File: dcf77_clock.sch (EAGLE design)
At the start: 42 parts, among them IC1 7805DT, IC2 ATMEGA48/88/168-AU, J2 DCJ0202, Q1 32.768kHz, Q2 IRLML6244TRPBF, SW1 EC12E_SW, U1 LCD-16X2SILK, U2 DS1307SO8

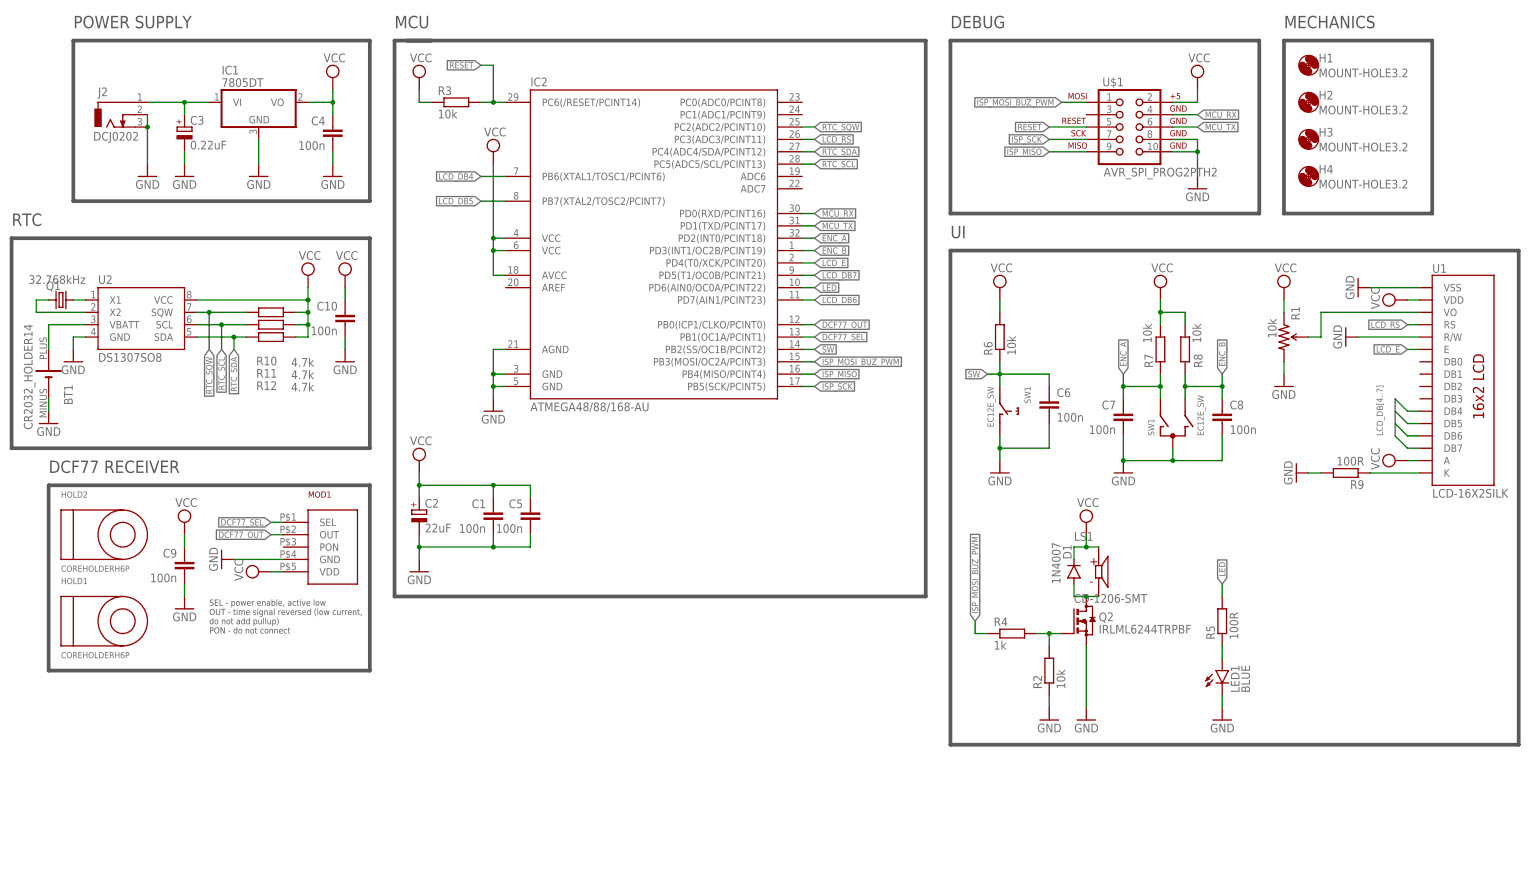
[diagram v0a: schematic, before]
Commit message: Finish signal and VCC routing
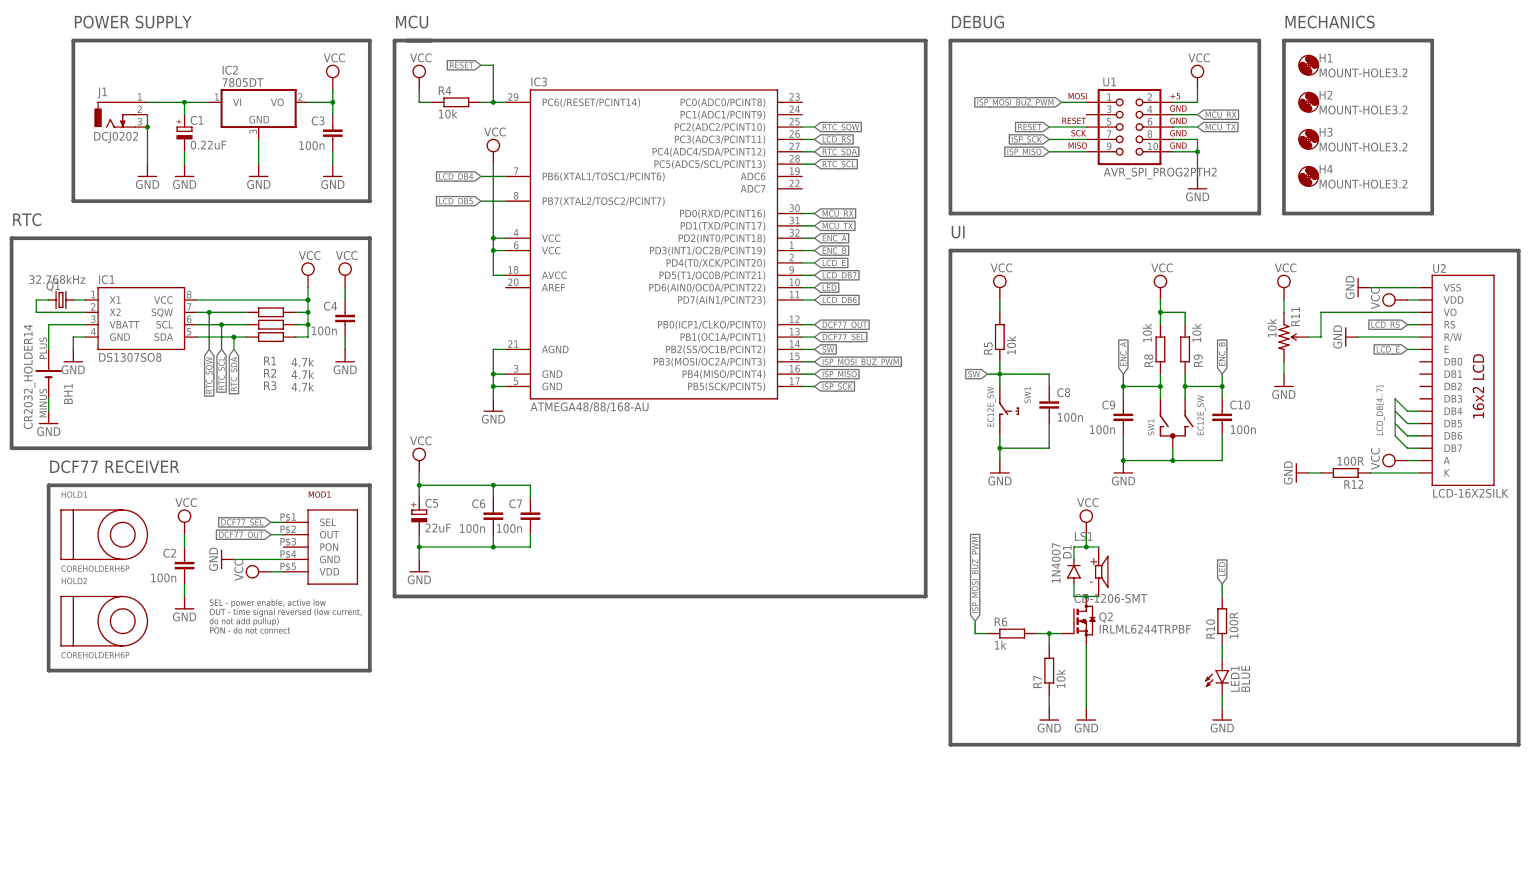
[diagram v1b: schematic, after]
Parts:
- removed U$1: AVR_SPI_PROG2PTH2, SparkFun:AVR_SPI_PROG2PTH2
- added IC3: ATMEGA48/88/168-AU, atmega8:ATMEGA48/88/168-AU
- C1: value 100n -> 0.22uF; device rcl:C-EUC0805K -> rcl:CPOL-EUSMCZ
- C2: value 22uF -> 100n; device rcl:CPOL-EUUD-4X5,8 -> rcl:C-EUC0805K
- C3: value 0.22uF -> 100n; device rcl:CPOL-EUSMCZ -> rcl:C-EUC0805K
- C5: value 100n -> 22uF; device rcl:C-EUC0805K -> rcl:CPOL-EUUD-4X5,8
- IC1: value 7805DT -> DS1307SO8; device linear:7805DT -> SparkFun:DS1307SO8
- IC2: value ATMEGA48/88/168-AU -> 7805DT; device atmega8:ATMEGA48/88/168-AU -> linear:7805DT
- R1: value 10k -> 4.7k; device SparkFun:TRIMPOTPTH -> rcl:R-EU_M0805
- R10, R12: value 4.7k -> 100R
- R11: value 4.7k -> 10k; device rcl:R-EU_M0805 -> SparkFun:TRIMPOTPTH
- R2, R3: value 10k -> 4.7k
- R4: value 1k -> 10k
- R5, R9: value 100R -> 10k
- R6: value 10k -> 1k
- U1: value LCD-16X2SILK -> AVR_SPI_PROG2PTH2; device SparkFun:LCD-16X2SILK -> SparkFun:AVR_SPI_PROG2PTH2
- U2: value DS1307SO8 -> LCD-16X2SILK; device SparkFun:DS1307SO8 -> SparkFun:LCD-16X2SILK
- renumbered BT1 to BH1, J2 to J1
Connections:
- net DCF77_OUT: now also IC3.PB0(ICP1/CLKO/PCINT0); no longer IC2.PB0(ICP1/CLKO/PCINT0)
- net DCF77_SEL: now also IC3.PB1(OC1A/PCINT1); no longer IC2.PB1(OC1A/PCINT1)
- net ENC_A: now also C9.1, IC3.PD2(INT0/PCINT18), R8.1; no longer C7.1, IC2.PD2(INT0/PCINT18), R7.1
- net ENC_B: now also C10.1, IC3.PD3(INT1/OC2B/PCINT19), R9.1; no longer C8.1, IC2.PD3(INT1/OC2B/PCINT19), R8.1
- net GND: now also C1.-, C2.2, C3.2, C5.-, IC2.GND, IC3.AGND, IC3.GND@1, IC3.GND@2, R11.CW, R12.2, R7.1, U1.10, U1.8, U2.R/W, U2.VSS; no longer C1.2, C2.-, C3.-, C5.2, IC2.AGND, IC2.GND@1, IC2.GND@2, R1.CW, R2.1, R9.2, U$1.10, U$1.8, U1.R/W, U1.VSS, U2.GND
- net ISP_MISO: now also IC3.PB4(MISO/PCINT4), U1.9; no longer IC2.PB4(MISO/PCINT4), U$1.9
- net ISP_MOSI_BUZ_PWM: now also IC3.PB3(MOSI/OC2A/PCINT3), R6.1, U1.1; no longer IC2.PB3(MOSI/OC2A/PCINT3), R4.1, U$1.1
- net ISP_SCK: now also IC3.PB5(SCK/PCINT5), U1.7; no longer IC2.PB5(SCK/PCINT5), U$1.7
- net LCD_DB4: now also IC3.PB6(XTAL1/TOSC1/PCINT6), U2.DB4; no longer IC2.PB6(XTAL1/TOSC1/PCINT6), U1.DB4
- net LCD_DB5: now also IC3.PB7(XTAL2/TOSC2/PCINT7), U2.DB5; no longer IC2.PB7(XTAL2/TOSC2/PCINT7), U1.DB5
- net LCD_DB6: now also IC3.PD7(AIN1/PCINT23), U2.DB6; no longer IC2.PD7(AIN1/PCINT23), U1.DB6
- net LCD_DB7: now also IC3.PD5(T1/OC0B/PCINT21), U2.DB7; no longer IC2.PD5(T1/OC0B/PCINT21), U1.DB7
- net LCD_E: now also IC3.PD4(T0/XCK/PCINT20), U2.E; no longer IC2.PD4(T0/XCK/PCINT20), U1.E
- net LCD_RS: now also IC3.PC3(ADC3/PCINT11), U2.RS; no longer IC2.PC3(ADC3/PCINT11), U1.RS
- net LED: now also IC3.PD6(AIN0/OC0A/PCINT22), R10.2; no longer IC2.PD6(AIN0/OC0A/PCINT22), R5.2
- net MCU_RX: now also IC3.PD0(RXD/PCINT16), U1.4; no longer IC2.PD0(RXD/PCINT16), U$1.4
- net MCU_TX: now also IC3.PD1(TXD/PCINT17), U1.6; no longer IC2.PD1(TXD/PCINT17), U$1.6
- net N$1: now also C1.+, IC2.VI; no longer C3.+, IC1.VI
- net N$10: now also IC1.X1; no longer U2.X1
- net N$11: now also IC1.X2; no longer U2.X2
- net N$12: now also IC1.VBATT; no longer U2.VBATT
- net N$3: now also R6.2, R7.2; no longer R2.2, R4.2
- net N$4: now also R10.1; no longer R5.1
- net N$7: now also R11.WIPER, U2.VO; no longer R1.WIPER, U1.VO
- net N$9: now also R12.1, U2.K; no longer R9.1, U1.K
- net RESET: now also IC3.PC6(/RESET/PCINT14), R4.2, U1.5; no longer IC2.PC6(/RESET/PCINT14), R3.2, U$1.5
- net RTC_SCL: now also IC1.SCL, IC3.PC5(ADC5/SCL/PCINT13), R2.2; no longer IC2.PC5(ADC5/SCL/PCINT13), R11.2, U2.SCL
- net RTC_SDA: now also IC1.SDA, IC3.PC4(ADC4/SDA/PCINT12), R3.2; no longer IC2.PC4(ADC4/SDA/PCINT12), R12.2, U2.SDA
- net RTC_SQW: now also IC1.SQW, IC3.PC2(ADC2/PCINT10), R1.2; no longer IC2.PC2(ADC2/PCINT10), R10.2, U2.SQW
- net SW: now also C8.1, IC3.PB2(SS/OC1B/PCINT2), R5.1; no longer C6.1, IC2.PB2(SS/OC1B/PCINT2), R6.1
- net VCC: now also C2.1, C3.1, C5.+, C6.1, C7.1, IC1.VCC, IC2.VO, IC3.AVCC, IC3.VCC@1, IC3.VCC@2, R1.1, R11.CCW, R2.1, R4.1, R5.2, R9.2, U1.2, U2.A, U2.VDD; no longer C1.1, C10.1, C2.+, C5.1, C9.1, IC1.VO, IC2.AVCC, IC2.VCC@1, IC2.VCC@2, R1.CCW, R10.1, R11.1, R12.1, R6.2, R7.2, U$1.2, U1.A, U1.VDD, U2.VCC
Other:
- moved on the sheet: C10, C4, C6, C7, C8, C9, HOLD1, HOLD2, R10, R12, R2, R3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

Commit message: Add BOM
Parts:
- U2: value LCD-16X2SILK -> LCD-16X2UPPERHOLES; device SparkFun:LCD-16X2SILK -> dcf77:LCD-16X2UPPERHOLES
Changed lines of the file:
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@@
 <grid distance="0.1" unitdist="inch" unit="inch" style="lines" multiple="1" display="yes" altdistance="0.01" altunitdist="inch" altunit="inch"/>
 <layers>
-<layer number="1" name="Top" color="4" fill="1" visible="no" active="no"/>
-<layer number="16" name="Bottom" color="1" fill="1" visible="no" active="no"/>
-<layer number="17" name="Pads" color="2" fill="1" visible="no" active="no"/>
-<layer number="18" name="Vias" color="2" fill="1" visible="no" active="no"/>
-<layer number="19" name="Unrouted" color="6" fill="1" visible="no" active="no"/>
-<layer number="20" name="Dimension" color="24" fill="1" visible="no" active="no"/>
-<layer number="21" name="tPlace" color="7" fill="1" visible="no" active="no"/>
-<layer number="22" name="bPlace" color="7" fill="1" visible="no" active="no"/>
-<layer number="23" name="tOrigins" color="15" fill="1" visible="no" active="no"/>
-<layer number="24" name="bOrigins" color="15" fill="1" visible="no" active="no"/>
-<layer number="25" name="tNames" color="7" fill="1" visible="no" active="no"/>
-<layer number="26" name="bNames" color="7" fill="1" visible="no" active="no"/>
-<layer number="27" name="tValues" color="7" fill="1" visible="no" active="no"/>
-<layer number="28" name="bValues" color="7" fill="1" visible="no" active="no"/>
+<layer number="1" name="Top" color="4" fill="1" visible="yes" active="no"/>
+<layer number="16" name="Bottom" color="1" fill="1" visible="yes" active="no"/>
+<layer number="17" name="Pads" color="2" fill="1" visible="yes" active="no"/>
+<layer number="18" name="Vias" color="2" fill="1" visible="yes" active="no"/>
+<layer number="19" name="Unrouted" color="6" fill="1" visible="yes" active="no"/>
+<layer number="20" name="Dimension" color="24" fill="1" visible="yes" active="no"/>
+<layer number="21" name="tPlace" color="7" fill="1" visible="yes" active="no"/>
+<layer number="22" name="bPlace" color="7" fill="1" visible="yes" active="no"/>
+<layer number="23" name="tOrigins" color="15" fill="1" visible="yes" active="no"/>
+<layer number="24" name="bOrigins" color="15" fill="1" visible="yes" active="no"/>
+<layer number="25" name="tNames" color="7" fill="1" visible="yes" active="no"/>
+<layer number="26" name="bNames" color="7" fill="1" visible="yes" active="no"/>
+<layer number="27" name="tValues" color="7" fill="1" visible="yes" active="no"/>
+<layer number="28" name="bValues" color="7" fill="1" visible="yes" active="no"/>
 <layer number="29" name="tStop" color="7" fill="3" visible="no" active="no"/>
 <layer number="30" name="bStop" color="7" fill="6" visible="no" active="no"/>
@@
 <layer number="35" name="tGlue" color="7" fill="4" visible="no" active="no"/>
 <layer number="36" name="bGlue" color="7" fill="5" visible="no" active="no"/>
-<layer number="37" name="tTest" color="7" fill="1" visible="no" active="no"/>
-<layer number="38" name="bTest" color="7" fill="1" visible="no" active="no"/>
+<layer number="37" name="tTest" color="7" fill="1" visible="yes" active="no"/>
+<layer number="38" name="bTest" color="7" fill="1" visible="yes" active="no"/>
 <layer number="39" name="tKeepout" color="4" fill="11" visible="no" active="no"/>
 <layer number="40" name="bKeepout" color="1" fill="11" visible="no" active="no"/>
@@
 <layer number="44" name="Drills" color="7" fill="1" visible="no" active="no"/>
 <layer number="45" name="Holes" color="7" fill="1" visible="no" active="no"/>
-<layer number="46" name="Milling" color="3" fill="1" visible="no" active="no"/>
-<layer number="47" name="Measures" color="7" fill="1" visible="no" active="no"/>
-<layer number="48" name="Document" color="7" fill="1" visible="no" active="no"/>
-<layer number="49" name="Reference" color="7" fill="1" visible="no" active="no"/>
-<layer number="50" name="dxf" color="7" fill="1" visible="no" active="no"/>
-<layer number="51" name="tDocu" color="7" fill="1" visible="no" active="no"/>
-<layer number="52" name="bDocu" color="7" fill="1" visible="no" active="no"/>
-<layer number="53" name="tGND_GNDA" color="7" fill="9" visible="no" active="no"/>
-<layer number="54" name="bGND_GNDA" color="1" fill="9" visible="no" active="no"/>
-<layer number="56" name="wert" color="7" fill="1" visible="no" active="no"/>
+<layer number="46" name="Milling" color="3" fill="1" visible="yes" active="no"/>
+<layer number="47" name="Measures" color="7" fill="1" visible="yes" active="no"/>
+<layer number="48" name="Document" color="7" fill="1" visible="yes" active="no"/>
+<layer number="49" name="Reference" color="7" fill="1" visible="yes" active="no"/>
+<layer number="50" name="dxf" color="7" fill="1" visible="yes" active="no"/>
+<layer number="51" name="tDocu" color="7" fill="1" visible="yes" active="no"/>
+<layer number="52" name="bDocu" color="7" fill="1" visible="yes" active="no"/>
+<layer number="53" name="tGND_GNDA" color="7" fill="9" visible="yes" active="no"/>
+<layer number="54" name="bGND_GNDA" color="1" fill="9" visible="yes" active="no"/>
+<layer number="56" name="wert" color="7" fill="1" visible="yes" active="no"/>
 <layer number="88" name="SimResults" color="9" fill="1" visible="yes" active="yes"/>
 <layer number="89" name="SimProbes" color="9" fill="1" visible="yes" active="yes"/>
@@
 <parts>
 <part name="U1" library="SparkFun" deviceset="AVR_SPI_PROG2" device="PTH2"/>
-<part name="U2" library="SparkFun" deviceset="LCD-16X2" device="SILK"/>
+<part name="U2" library="dcf77" deviceset="LCD-16X2" device="UPPERHOLES"/>
 <part name="LED1" library="led" library_urn="urn:adsk.eagle:library:259" deviceset="LED" device="CHIP-LED0805" package3d_urn="urn:adsk.eagle:package:15818/2" value="BLUE"/>
 <part name="IC3" library="atmega8" deviceset="ATMEGA48/88/168" device="-AU"/>
@@
 <instance part="U2" gate="G$1" x="157.48" y="33.02" smashed="yes">
 <attribute name="NAME" x="149.86" y="56.388" size="1.778" layer="95"/>
-<attribute name="VALUE" x="149.86" y="10.16" size="1.778" layer="96"/>
+<attribute name="VALUE" x="134.62" y="10.16" size="1.778" layer="96"/>
 </instance>
 <instance part="LED1" gate="G$1" x="106.68" y="-25.4" smashed="yes">
@@
 </sheet>
 </sheets>
-<errors>
-</errors>
 </schematic>
 </drawing>

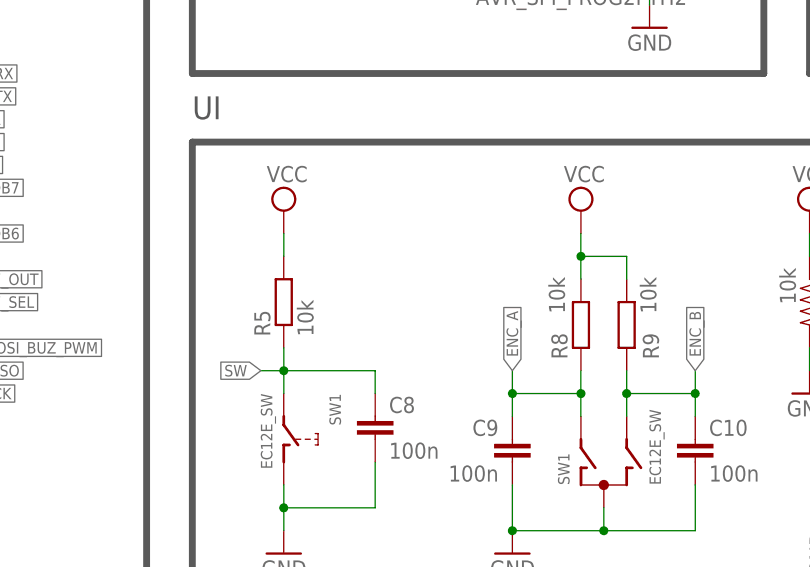
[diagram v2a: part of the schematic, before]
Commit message: Place hidden encoder pins and connect to GND
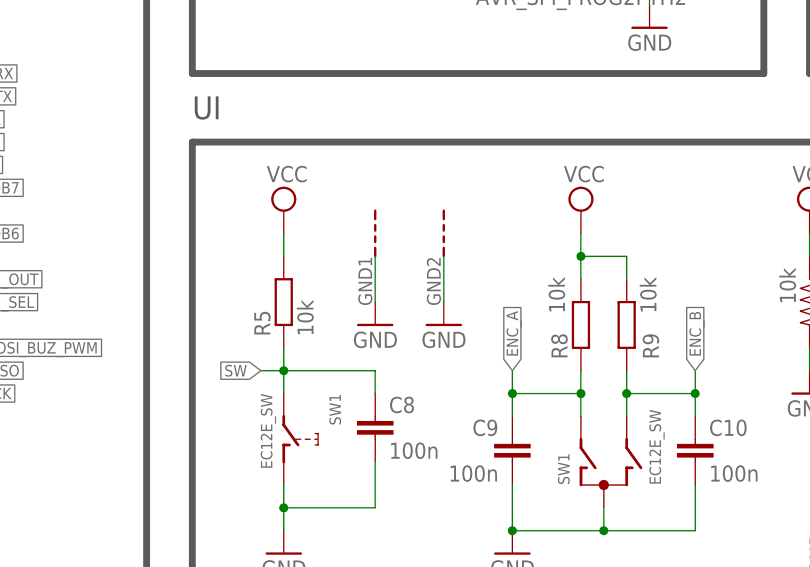
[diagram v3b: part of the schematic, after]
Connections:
- net GND: now also SW1G$3.G, SW1G$4.G
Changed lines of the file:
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@@
 <part name="GND21" library="supply1" library_urn="urn:adsk.eagle:library:371" deviceset="GND" device=""/>
 <part name="LS1" library="CD-1206-SMT" deviceset="CD-1206-SMT" device=""/>
+<part name="GND22" library="supply1" library_urn="urn:adsk.eagle:library:371" deviceset="GND" device=""/>
+<part name="GND23" library="supply1" library_urn="urn:adsk.eagle:library:371" deviceset="GND" device=""/>
 </parts>
 <sheets>
@@
 <attribute name="VALUE" x="76.17583125" y="-11.46021875" size="1.78646875" layer="96"/>
 </instance>
+<instance part="SW1" gate="G$3" x="71.12" y="48.26" smashed="yes" rot="R90"/>
+<instance part="SW1" gate="G$4" x="78.74" y="48.26" smashed="yes" rot="R90"/>
+<instance part="GND22" gate="1" x="78.74" y="40.64" smashed="yes" rot="MR0">
+<attribute name="VALUE" x="81.28" y="38.1" size="1.778" layer="96" rot="MR0"/>
+</instance>
+<instance part="GND23" gate="1" x="71.12" y="40.64" smashed="yes" rot="MR0">
+<attribute name="VALUE" x="73.66" y="38.1" size="1.778" layer="96" rot="MR0"/>
+</instance>
 </instances>
 <busses>
@@
 <wire x1="-73.66" y1="40.64" x2="-73.66" y2="43.18" width="0.1524" layer="91"/>
 </segment>
+<segment>
+<pinref part="SW1" gate="G$4" pin="G"/>
+<wire x1="78.74" y1="48.26" x2="78.74" y2="43.18" width="0.1524" layer="91"/>
+<pinref part="GND22" gate="1" pin="GND"/>
+</segment>
+<segment>
+<pinref part="SW1" gate="G$3" pin="G"/>
+<wire x1="71.12" y1="48.26" x2="71.12" y2="43.18" width="0.1524" layer="91"/>
+<pinref part="GND23" gate="1" pin="GND"/>
+</segment>
 </net>
